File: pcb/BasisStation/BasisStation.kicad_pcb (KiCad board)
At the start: 2 copper layers, 160 x 135 mm, 80 parts, among them J1 12401598E4-2A, J6 61200621621, Q1 BC337, Q2 BC337, Q3 BC337, Q4 BC337, T1 7499011121A, U1 D3V3XA4B10LP, U6 ESP32-S3-WROOM-1U-N16R8, U7 W5500, Y1 25 MHz

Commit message: v0.00.001 feat(SHBS-21): Versorgungsleitungen aufgeweitet, DRC-Ausschlüsse J_PWR1 (Nachtrag)
Nachtrag zu b0bc21b: Dieser Commit enthielt versehentlich nur das
Verschieben der Task-Datei 0048. Hier folgen die eigentlichen Änderungen:
VBUS-Hauptpfad A9 → F1 und B.Cu-Brücke 0,6 mm (Pad-Feld 0,2 mm),
A4-Zweig 0,3 mm wegen CC1, +5V zu D12 als 0,6-mm-Leiterbahnen statt
Grafiklinien, vier DRC-Ausschlüsse an J_PWR1, power_supply.md und
memory.md aktualisiert.

Co-Authored-By: Claude Opus 5.5 <noreply@anthropic.com>
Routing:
- net /Stromversorgung/+5V: track 12.2 -> 20.4 mm
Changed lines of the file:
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@@
-	)
-	(gr_line
-		(start 58.5 46.5)
-		(end 58 46)
-		(stroke
-			(width 0.2)
-			(type default)
-		)
-		(layer "F.Cu")
-		(net 4)
-	)
-	(gr_line
-		(start 66 46.5)
-		(end 58.5 46.5)
-		(stroke
-			(width 0.2)
-			(type default)
-		)
-		(layer "F.Cu")
-		(net 4)
 	)
 	(gr_line
@@
 		(start 58 46)
 		(end 58 44)
-		(width 0.2)
+		(width 0.6)
 		(layer "F.Cu")
 		(net 4)
@@
 		(start 66.95 50.45)
 		(end 66 51.4)
+		(width 0.6)
+		(layer "F.Cu")
+		(net 4)
+	)
+	(segment
+		(start 66 46.5)
+		(end 58.5 46.5)
+		(width 0.6)
+		(layer "F.Cu")
+		(net 4)
+	)
+	(segment
+		(start 58.5 46.5)
+		(end 58 46)
 		(width 0.6)
 		(layer "F.Cu")
@@
 	(segment
 		(start 73.75 36.52)
-		(end 73.75 38.75)
+		(end 73.75 37.4)
 		(width 0.2)
 		(layer "F.Cu")
@@
 		(start 71.25 37.75)
 		(end 69.5 39.5)
-		(width 0.2)
+		(width 0.6)
+		(layer "F.Cu")
+		(net 23)
+	)
+	(segment
+		(start 71.25 37.4)
+		(end 71.25 37.75)
+		(width 0.6)
 		(layer "F.Cu")
 		(net 23)
@@
 		(start 67 39.5)
 		(end 66 40.5)
-		(width 0.2)
+		(width 0.6)
 		(layer "F.Cu")
 		(net 23)
@@
 	(segment
 		(start 71.25 36.52)
-		(end 71.25 37.75)
+		(end 71.25 37.4)
 		(width 0.2)
 		(layer "F.Cu")
@@
 		(start 70 39.5)
 		(end 69.5 39.5)
-		(width 0.2)
+		(width 0.6)
 		(layer "F.Cu")
 		(net 23)
@@
 		(start 66 40.5)
 		(end 66 42.1)
-		(width 0.2)
+		(width 0.6)
+		(layer "F.Cu")
+		(net 23)
+	)
+	(segment
+		(start 73.75 37.4)
+		(end 73.75 38.75)
+		(width 0.3)
 		(layer "F.Cu")
 		(net 23)
@@
 		(start 73.75 38.75)
 		(end 73 39.5)
-		(width 0.2)
+		(width 0.3)
 		(layer "F.Cu")
 		(net 23)
@@
 		(start 69.5 39.5)
 		(end 67 39.5)
-		(width 0.2)
+		(width 0.6)
 		(layer "F.Cu")
 		(net 23)
@@
 		(start 73 39.5)
 		(end 70 39.5)
-		(width 0.2)
+		(width 0.6)
 		(layer "B.Cu")
 		(net 23)

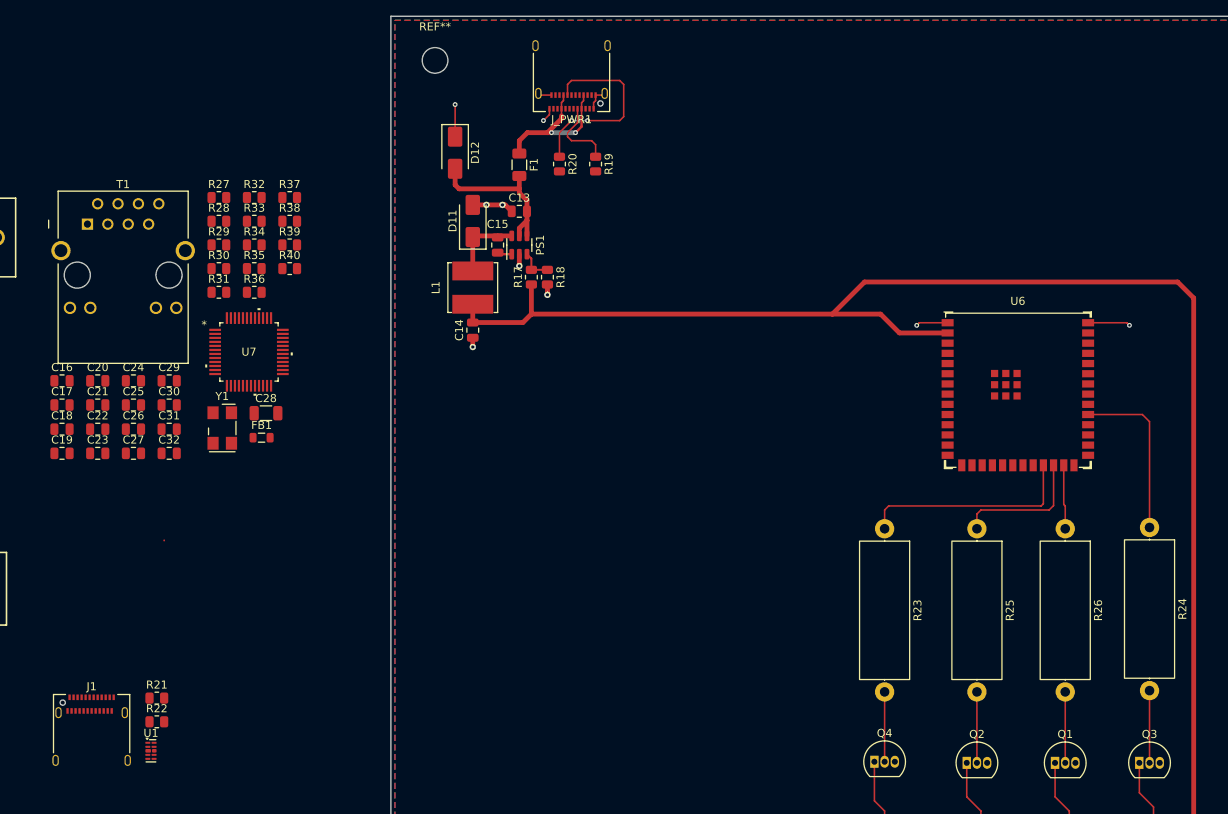
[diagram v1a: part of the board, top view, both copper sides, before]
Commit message: v0.00.001 feat(SHBS-22): Debug-USB J1/U1 fertig verdrahtet
Durchgänge unter dem ESD-Array U1 ergänzt (10→1 USB−, 9→2 USB+,
7→4 VBUS_J1; 0,15 mm neben den GND-Pads). Brücken im Pad-Feld von J1:
D+ B6→A6 auf F.Cu, D− B7→A7 über Via und B.Cu (Kreuzung mit D+),
VBUS_J1 B4→A9 und B9→A4, Gruppe A4/B9 über B.Cu. DRC: keine offene
Verbindung mehr an J1/U1. hardware.md und Review-Report ergänzt.

Co-Authored-By: Claude Opus 5.5 <noreply@anthropic.com>
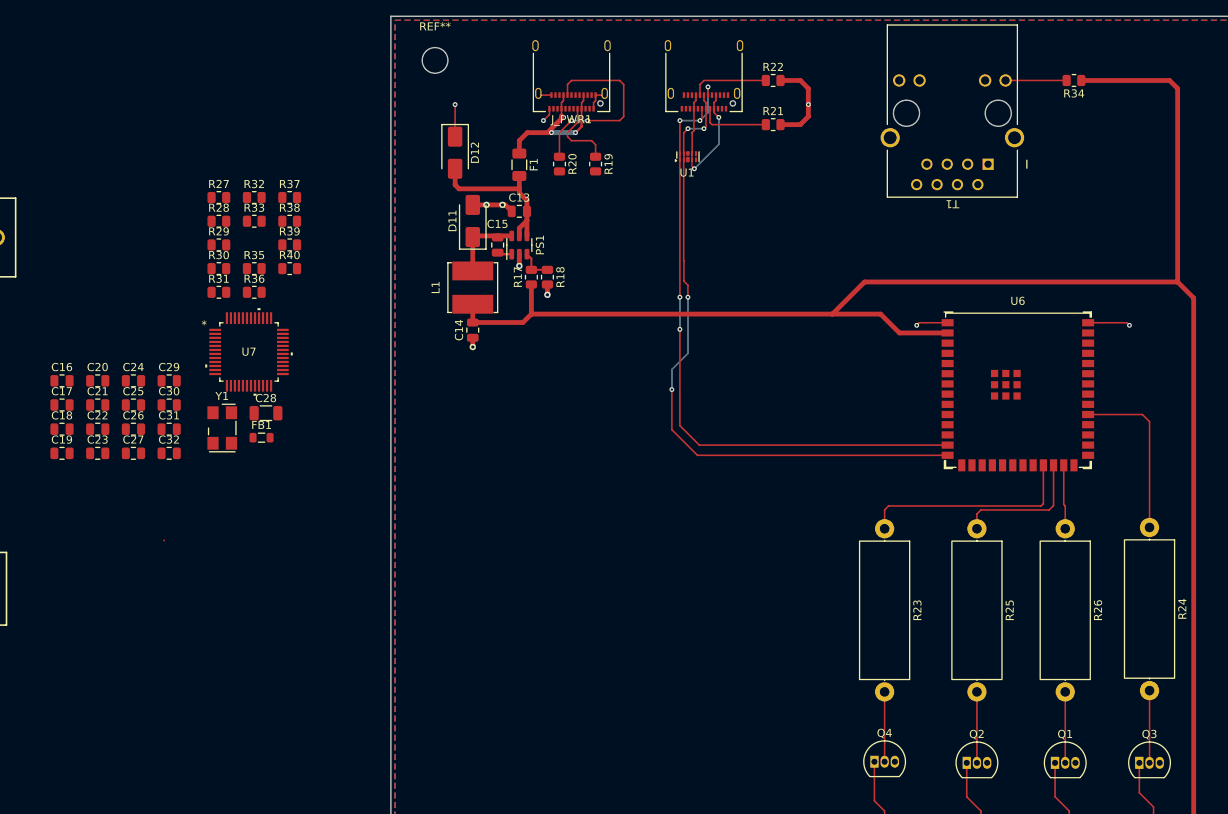
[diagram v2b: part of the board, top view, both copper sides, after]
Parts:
- moved J1 113.0 mm to (89.0, 31.5), turned to 180 degrees
- moved T1 112.4 mm to (124.4, 43.4), turned to 180 degrees
- moved R22 110.8 mm to (97.6, 33.0)
- moved R21 104.9 mm to (97.6, 38.5)
- moved R34 104.1 mm to (135.1, 33.0), turned to 180 degrees
- moved U1 99.7 mm to (87.0, 42.5), turned to 90 degrees
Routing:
- net USB-: track 0.00 -> 82.1 mm, vias 0 -> 5
- net USB+: track 0.00 -> 80.8 mm, vias 0 -> 4
- net +3V3: track 259.2 -> 295.7 mm
- net /Debugging/VBUS_J1: track 0.00 -> 20.3 mm, vias 0 -> 2
- net GND: track 28.9 -> 40.2 mm, vias 9 -> 10
- net Net-(J1-CC2): track 0.00 -> 9.73 mm
- net Net-(J1-CC1): track 0.00 -> 8.79 mm
- net Net-(T1-LED1_Y+): track 0.00 -> 7.61 mm

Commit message: v0.00.001 feat(SHBS-23): Gesamt-Layout platziert und geroutet, DRC sauber
U6 nach rechts oben (U.FL zur Ecke), W5500 mit Beschaltung neben T1
(Ethernet-Teil SHBS-10), S2/R9/J6/Puffer-C platziert. Passive um U7 im
Raster 3,5 mm für Handlötung. Ethernet-Paare und R36/R37 von Hand, Rest
mit Freerouting, GND-Pins von U7/J1 und Masseinseln über Vias an die
Rückseitenmasse. Chassis-Zone unter T1. Obere Kante auf y 27,45, damit
J_PWR1/J1/T1 für das Gehäuse 1,2–1,3 mm überstehen. H1–H4 als
Montagelöcher (nur Platine). DRC-Regel für das U1-Landepattern
(kicad_dru), 11 neue begründete Ausschlüsse. DRC: 0 offene
Verbindungen, 0 Paritätsfehler. hardware.md, memory.md, Renderbilder.

Co-Authored-By: Claude Opus 5.5 <noreply@anthropic.com>
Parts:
- moved J6 211.1 mm to (203.0, 64.0), turned to 90 degrees
- moved C10 190.4 mm to (168.0, 62.0)
- moved C12 190.4 mm to (168.0, 71.0)
- moved C7 181.7 mm to (160.0, 81.0)
- moved C8 180.4 mm to (172.5, 44.0)
- moved R9 180.0 mm to (151.5, 29.5)
- moved S2 173.2 mm to (168.0, 33.5)
- moved C16 144.4 mm to (151.8, 48.5), turned to 90 degrees
- moved C26 141.4 mm to (157.8, 56.0), turned to 90 degrees
- moved C22 139.6 mm to (151.5, 55.5), turned to 90 degrees
- moved C25 137.5 mm to (154.3, 56.0), turned to 90 degrees
- moved C19 136.9 mm to (144.5, 59.5), turned to 90 degrees
- moved C23 133.2 mm to (144.5, 55.5), turned to 90 degrees
- moved C18 133.0 mm to (141.0, 59.5), turned to 90 degrees
- moved C27 131.6 mm to (148.0, 59.5), turned to 90 degrees
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- renumbered REF** to H1, REF** to H2, REF** to H3, REF** to H4
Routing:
- net +3V3: track 295.7 -> 445.7 mm, vias 0 -> 3
- net /Layout/EN: track 0.00 -> 129.9 mm
- net /Ethernet/+3V3A: track 0.00 -> 79.0 mm, vias 0 -> 3
- net Net-(U6-GPIO47/SPICLK_P/SUBSPICLK_P_DIFF): track 16.8 -> 85.5 mm
- net Net-(U6-GPIO21): track 27.2 -> 95.8 mm
- net Net-(U6-GPIO48/SPICLK_N/SUBSPICLK_N_DIFF): track 7.98 -> 75.8 mm
- net ETH_INT: track 0.00 -> 58.0 mm, vias 0 -> 2
- net ETH_RST: track 0.00 -> 54.5 mm, vias 0 -> 2
- net Net-(U6-GPIO38/FSPIWP/SUBSPIWP): track 21.2 -> 71.1 mm, vias 0 -> 1
- net ETH_MISO: track 0.00 -> 49.0 mm, vias 0 -> 2
- net ETH_SCLK: track 0.00 -> 46.9 mm, vias 0 -> 2
- net USB-: track 82.1 -> 126.1 mm, vias 5 -> 3
- net ETH_MOSI: track 0.00 -> 42.9 mm, vias 0 -> 2
- net ETH_SCSn: track 0.00 -> 42.3 mm, vias 0 -> 4
- net Net-(T1-LED2_G-): track 0.00 -> 42.1 mm, vias 0 -> 1
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- added copper zone on B.Cu, net /Ethernet/CHASSIS
- added copper zone on F.Cu, net /Ethernet/CHASSIS
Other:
- board size 160 x 135 mm -> 160 x 132.6 mm
